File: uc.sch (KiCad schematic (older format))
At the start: 15 parts

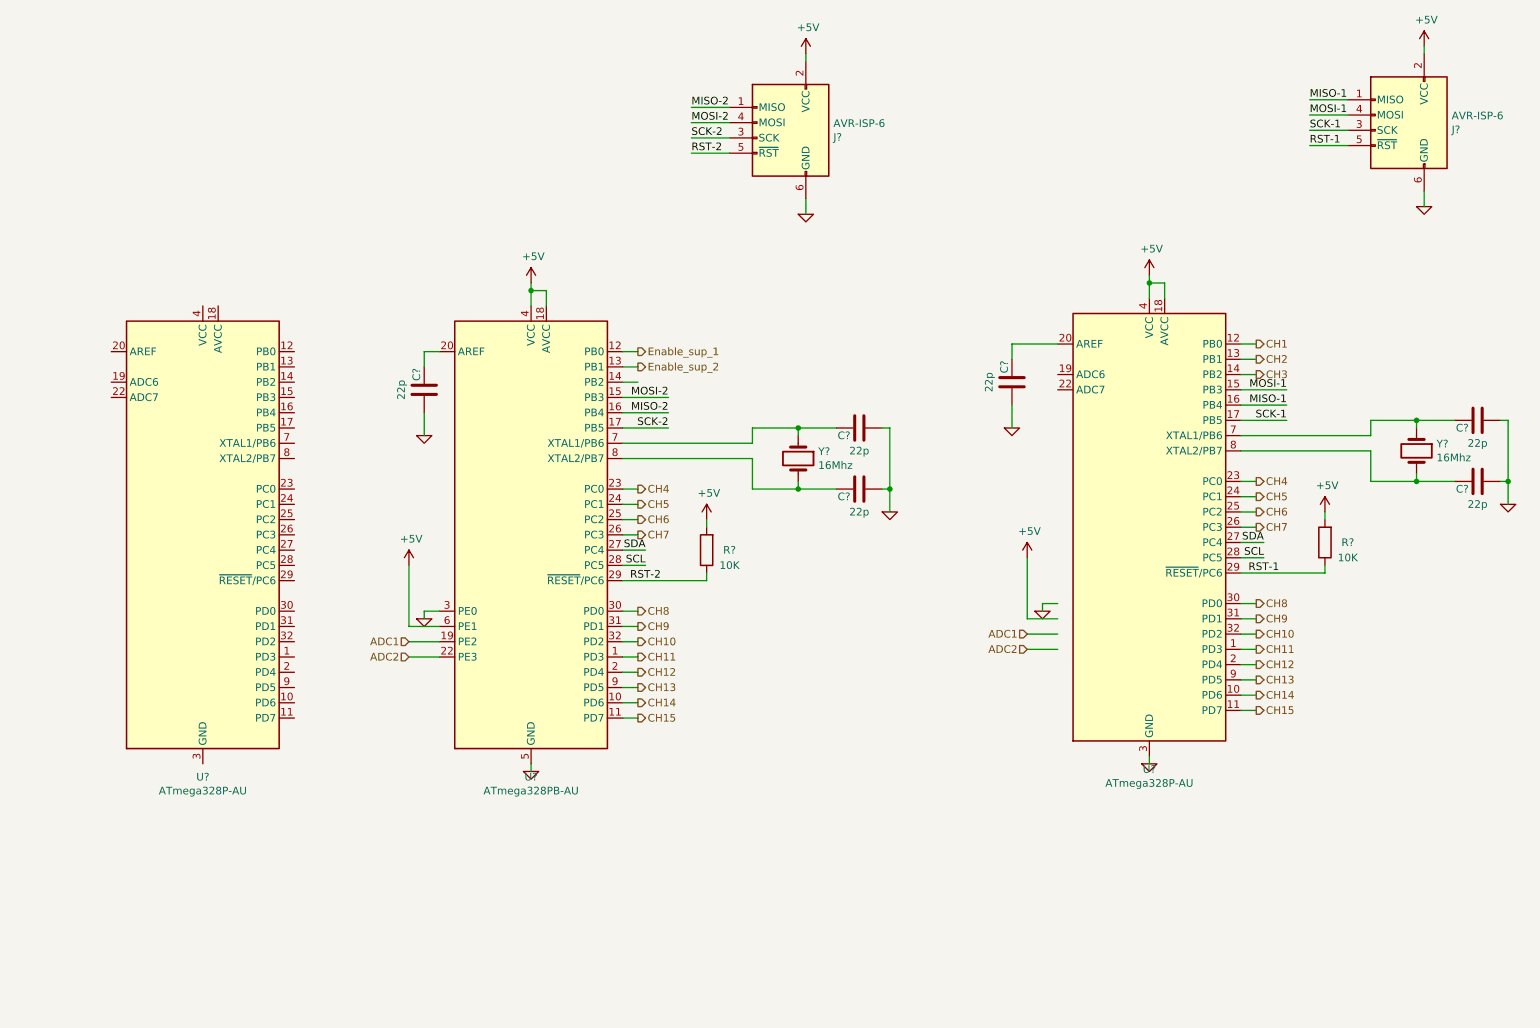
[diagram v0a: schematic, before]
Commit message: added uc part
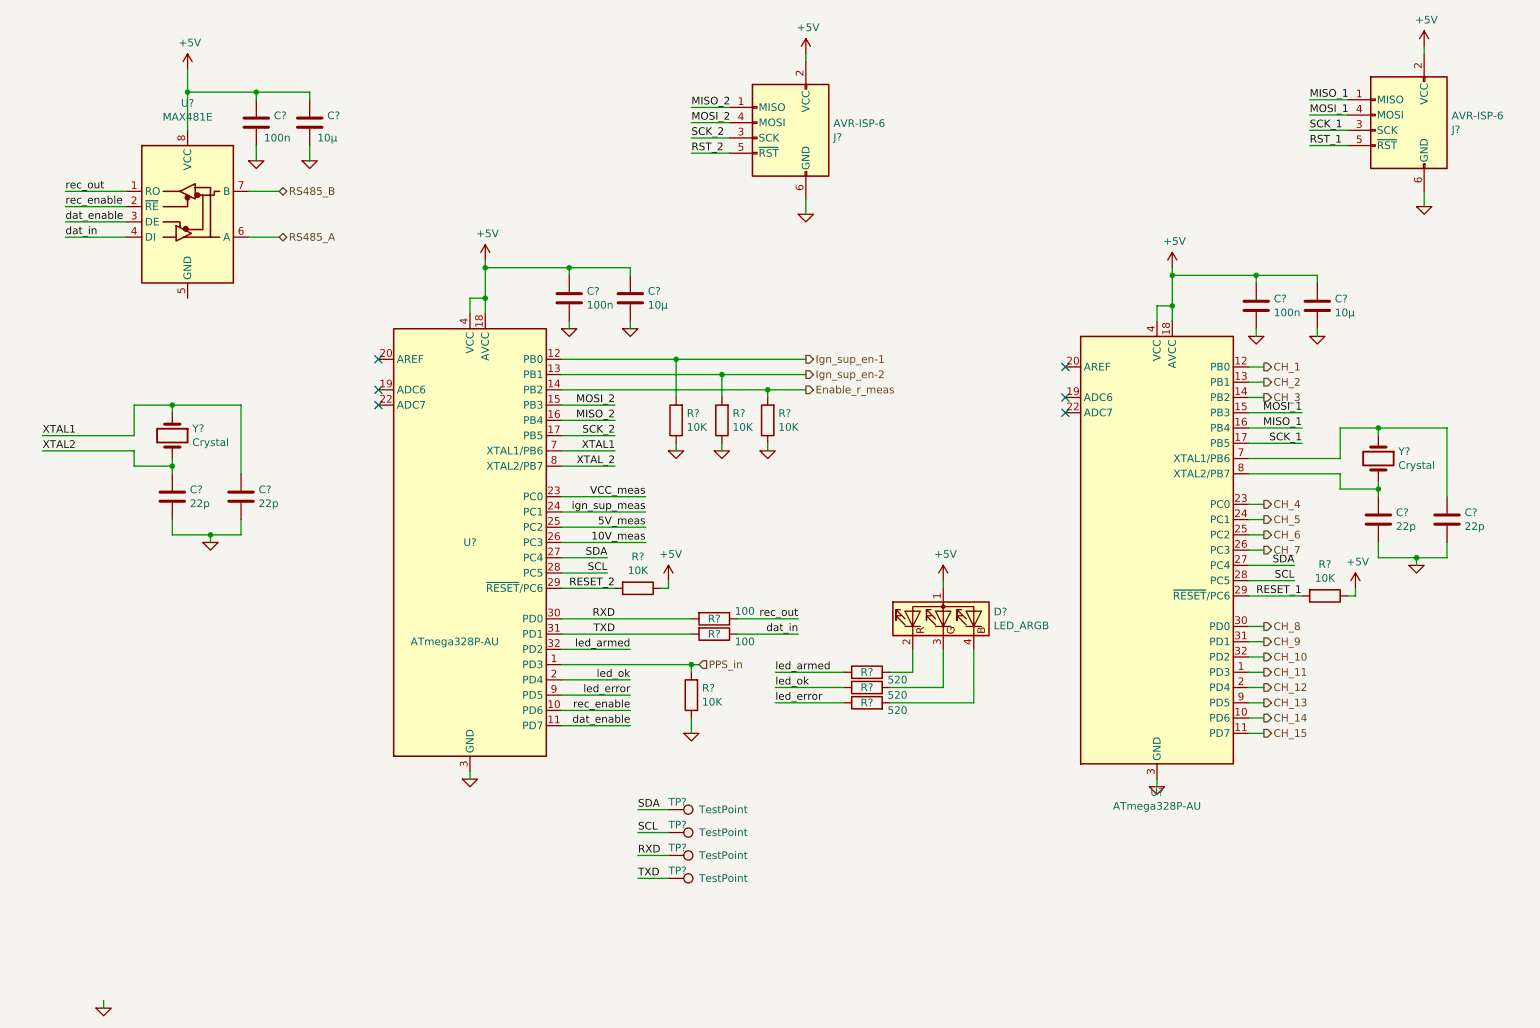
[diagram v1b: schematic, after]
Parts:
- removed C? (x6): 22p, symbol Device:C
- removed R? (x2): 10K, symbol Device:R
- removed U?: ATmega328PB-AU, Package_QFP:TQFP-32_7x7mm_P0.8mm, symbol MCU_Microchip_ATmega:ATmega328PB-AU
- removed U? (x2): ATmega328P-AU, Package_QFP:TQFP-32_7x7mm_P0.8mm, symbol MCU_Microchip_ATmega:ATmega328P-AU
- removed Y? (x2): 16Mhz, symbol Device:Crystal
- added C? (x4): 22p, symbol Device:C
- added C? (x3): 100n, symbol Device:C
- added C? (x3): 10µ, symbol Device:C
- added D?: LED_ARGB, symbol Device:LED_ARGB
- added R? (x6): 10K, symbol Device:R
- added R? (x3): 520, symbol Device:R
- added R? (x2): 100, symbol Device:R
- added TP? (x4): TestPoint, symbol Connector:TestPoint
- added U? (x2): ATmega328P-AU, Package_QFP:TQFP-32_7x7mm_P0.8mm, symbol MCU_Microchip_ATmega:ATmega328P-AU
- added U?: MAX481E, symbol Interface_UART:MAX481E
- added Y? (x2): Crystal, symbol Device:Crystal
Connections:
- net labels added: 10V_meas, 5V_meas, CH_1, CH_10, CH_11, CH_12, CH_13, CH_14, CH_15, CH_2, CH_3, CH_4, CH_5, CH_6, CH_7, CH_8, CH_9, Enable_r_meas, Ign_sup_en-1, Ign_sup_en-2, MISO_1, MISO_2, MOSI_1, MOSI_2, PPS_in, RESET_1, RESET_2, RS485_A, RS485_B, RST_1, RST_2, RXD, SCK_1, SCK_2, TXD, VCC_meas, XTAL1, XTAL2, XTAL_2, dat_enable, dat_in, ign_sup_meas, led_armed, led_error, led_ok, rec_enable, rec_out
- net labels removed: ADC1, ADC2, CH1, CH10, CH11, CH12, CH13, CH14, CH15, CH2, CH3, CH4, CH5, CH6, CH7, CH8, CH9, Enable_sup_1, Enable_sup_2, MISO-1, MISO-2, MOSI-1, MOSI-2, RST-1, RST-2, SCK-1, SCK-2
- wire segments 114 -> 159
- no-connect marks 0 -> 6

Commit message: added rs485 interface
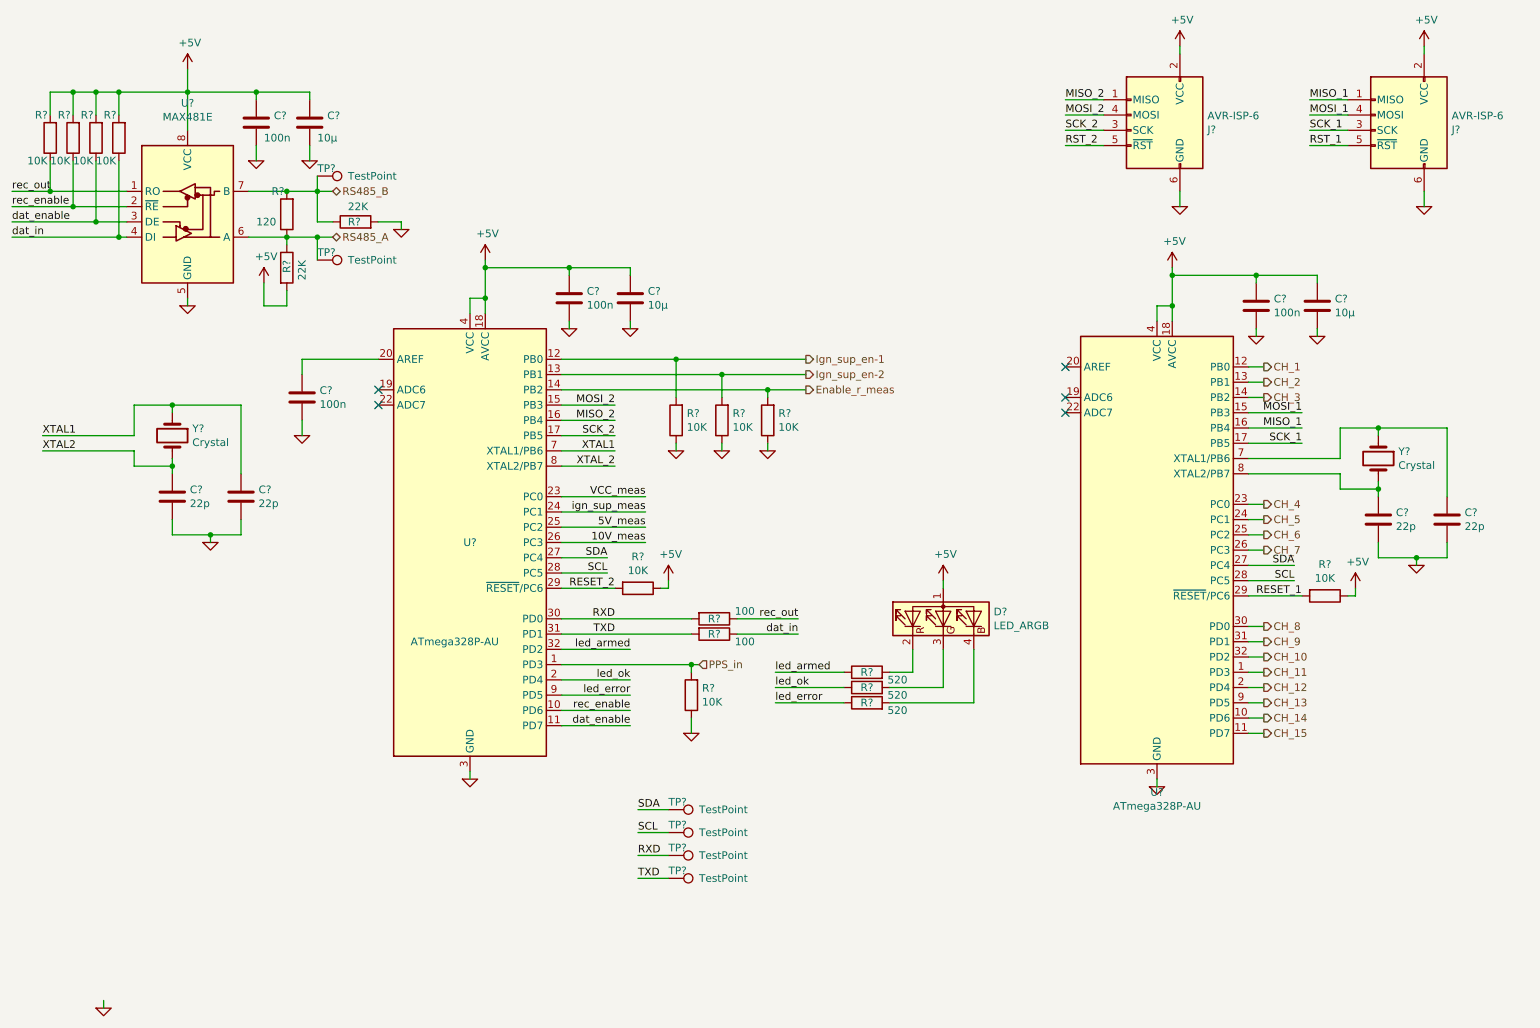
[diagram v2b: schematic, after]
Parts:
- added C?: 100n, symbol Device:C
- added R? (x4): 10K, symbol Device:R
- added R?: 120, symbol Device:R
- added R? (x2): 22K, symbol Device:R
- added TP? (x2): TestPoint, symbol Connector:TestPoint
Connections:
- net +5V: now also R?.2, R?.2, R?.2, R?.2, R?.2
- net GND: now also U?.5 (GND), C?.2, R?.2
- net RS485_A: now also R?.1, R?.1, TP?.1
- net RS485_B: now also R?.1, R?.2, TP?.1
- net dat_enable: now also R?.1
- net dat_in: now also R?.1
- net rec_enable: now also R?.1
- net rec_out: now also R?.1
- net at U?.20 (AREF): now also C?.1
- no-connect marks 6 -> 5
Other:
- moved on the sheet: J?

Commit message: finished schematic for review
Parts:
- removed R?: 10K, symbol Device:R
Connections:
- net Enable_r_meas renamed ADC_Ready
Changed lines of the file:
@@
 NoConn ~ 3250 3450
 Text HLabel 6050 3350 2    50   Output ~ 0
-Enable_r_meas
+ADC_Ready
 Text Label 1050 3650 0    50   ~ 0
 XTAL1
@@
 	-1   0    0    1
 $EndComp
-$Comp
-L Device:R R?
-U 1 1 5D2B7F9E
-P 5800 3550
-F 0 "R?" H 5730 3504 50  0000 R CNN
-F 1 "10K" H 5730 3595 50  0000 R CNN
-F 2 "" V 5730 3550 50  0001 C CNN
-F 3 "~" H 5800 3550 50  0001 C CNN
-	1    5800 3550
-	-1   0    0    1
-$EndComp
 Wire Wire Line
 	4450 3150 5200 3150
-Wire Wire Line
-	4450 3350 5800 3350
 Wire Wire Line
 	5200 3400 5200 3150
@@
 Wire Wire Line
 	5500 3250 6050 3250
-Wire Wire Line
-	5800 3400 5800 3350
-Connection ~ 5800 3350
-Wire Wire Line
-	5800 3350 6050 3350
 $Comp
 L daisy:GND #PWR?
@@
 	1    0    0    -1
 $EndComp
-$Comp
-L daisy:GND #PWR?
-U 1 1 5D2D4E8A
-P 5800 3750
-F 0 "#PWR?" H 5800 3750 30  0001 C CNN
-F 1 "GND" H 5800 3680 30  0001 C CNN
-F 2 "" H 5800 3750 60  0000 C CNN
-F 3 "" H 5800 3750 60  0000 C CNN
-	1    5800 3750
-	1    0    0    -1
-$EndComp
-Wire Wire Line
-	5800 3700 5800 3750
 Wire Wire Line
 	5500 3700 5500 3750
@@
 Wire Wire Line
 	2500 2650 2500 2800
+Text HLabel 4950 6100 0    50   Input ~ 0
+SDA
+Text HLabel 4950 6250 0    50   Input ~ 0
+SCL
+Wire Wire Line
+	4450 3350 6050 3350
 $EndSCHEMATC

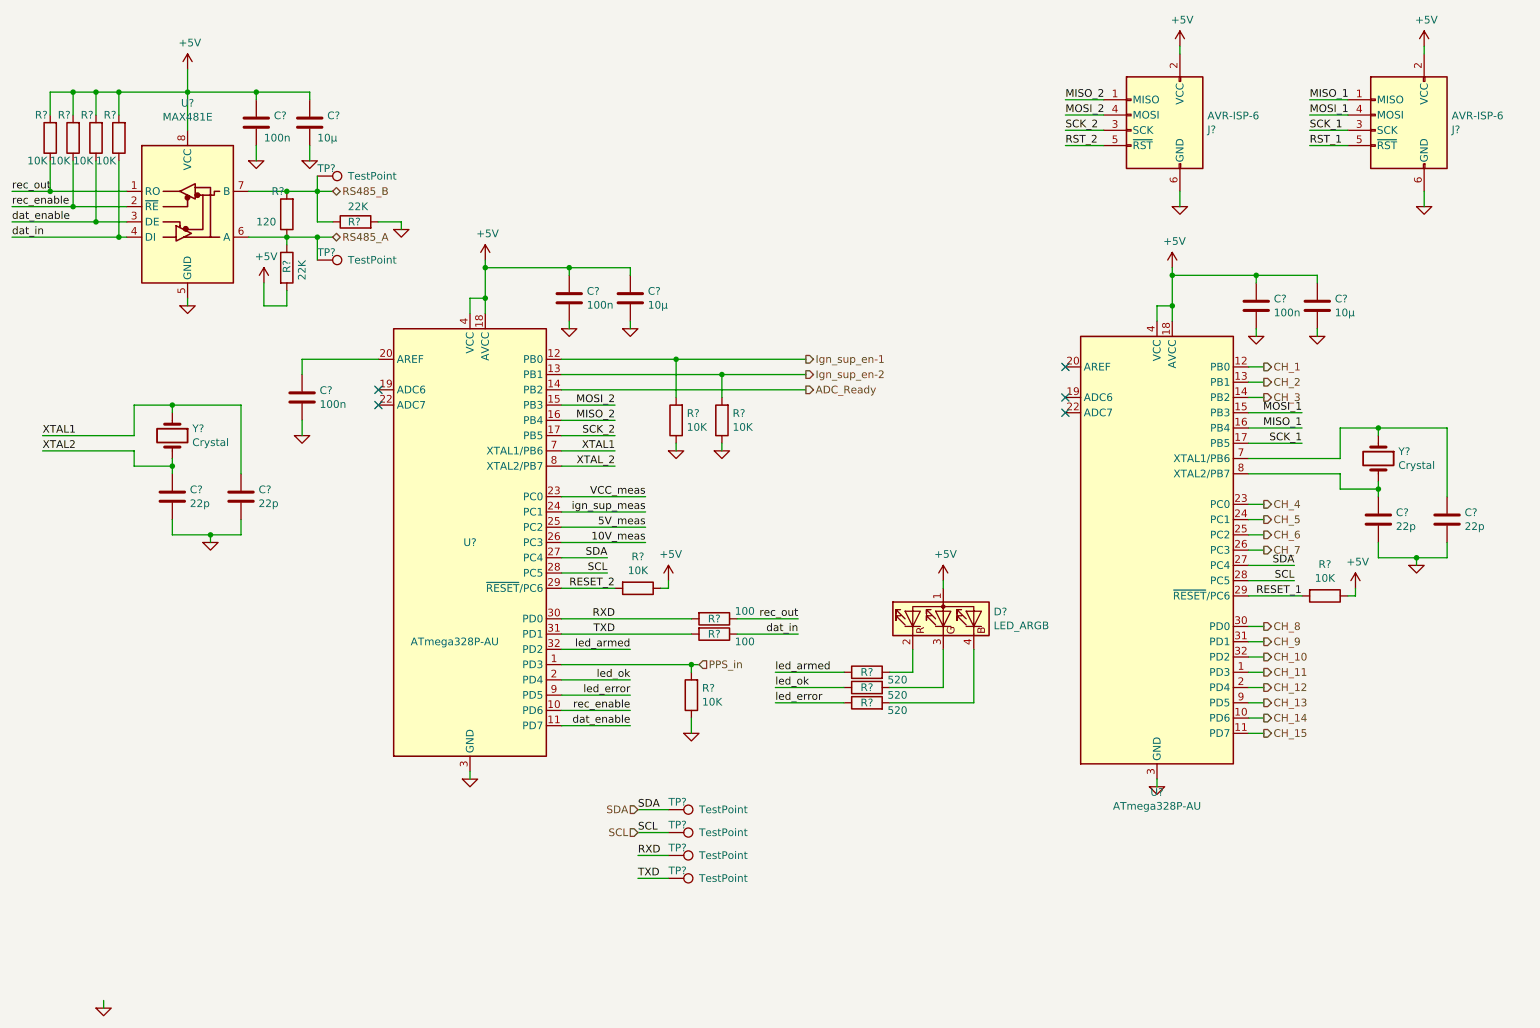
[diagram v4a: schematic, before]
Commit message: added pdf schematic
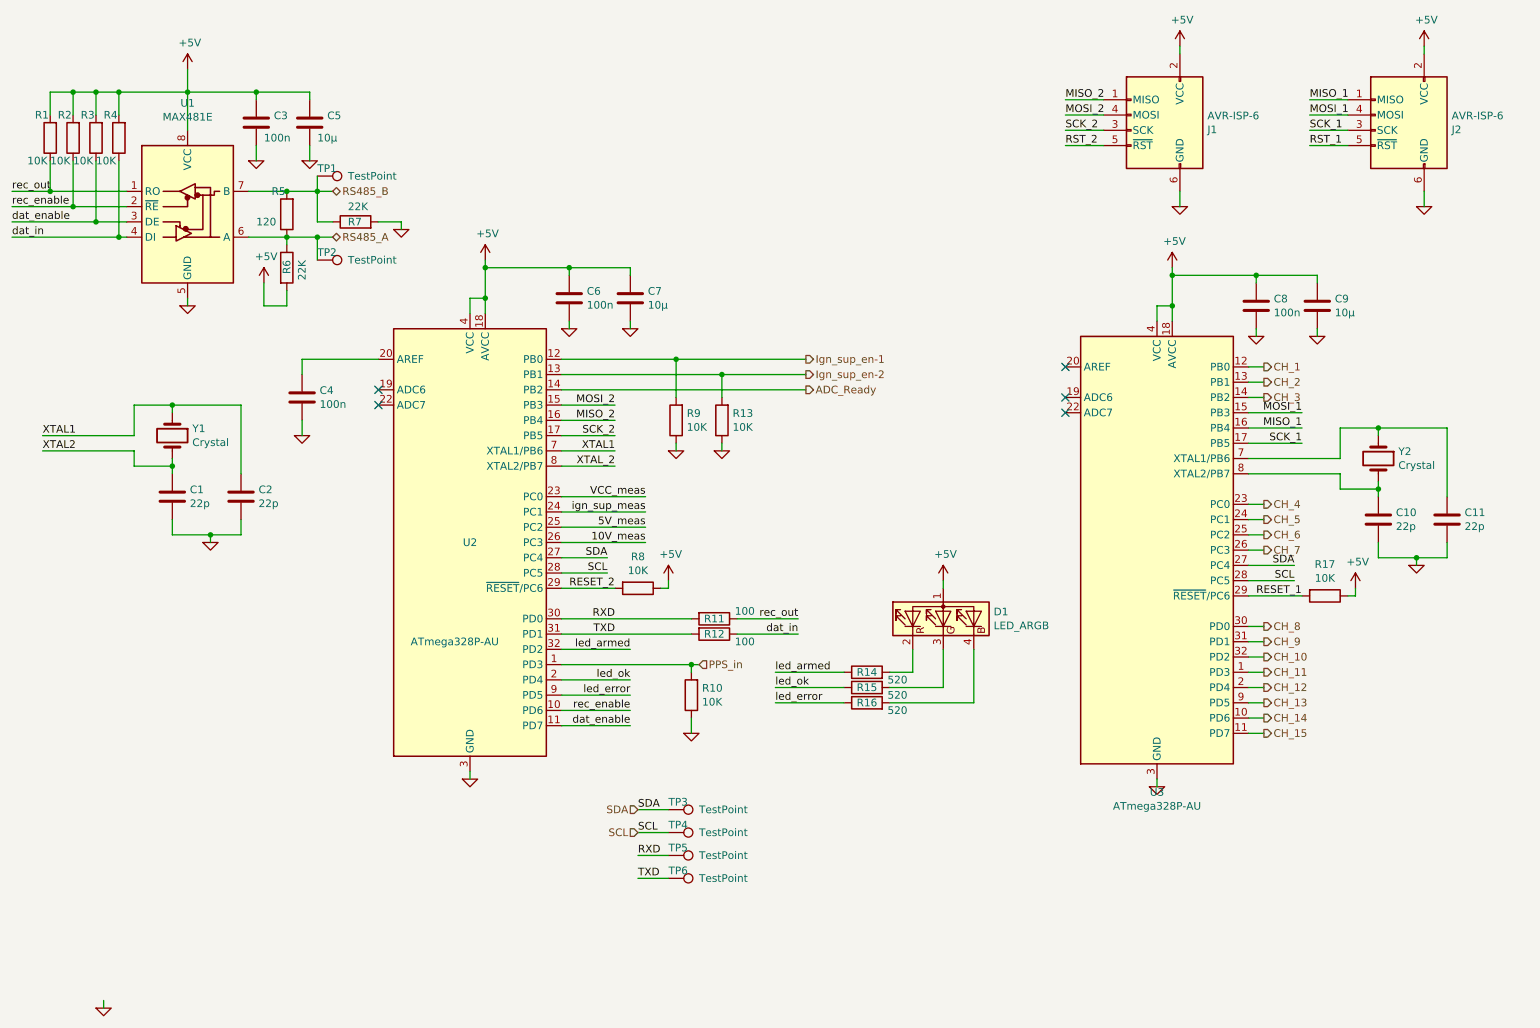
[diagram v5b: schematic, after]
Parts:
- gave numbers to parts that had none: 42
